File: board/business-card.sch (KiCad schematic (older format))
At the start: 36 parts, among them J1 Conn_01x06, SW1 SW_SPDT, SW2 Mutual_Capacitance_Button, SW3 Mutual_Capacitance_Button, SW4 Mutual_Capacitance_Button, SW5 Mutual_Capacitance_Button, SW6 Mutual_Capacitance_Button, SW7 Mutual_Capacitance_Button, U1 ATtiny1616-S

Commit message: Added through board footprint for XZCBD led.
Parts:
- BT1: mfg1 (none) -> Renata; mfg1pn (none) -> CR2016 MFR SM
- D1, D10, D11, D12, D13, D14, D15, D16, D17, D18, D19, D2, D20, D21, D22, D23, D24, D25, D3, D4, D5, D6, D7, D8, D9: footprint LED_SMD:LED_0603_1608Metric -> business-card:XZCBD53W-6_through_board_mount
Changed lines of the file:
@@
 F 2 "business-card:CR2016_MFR_SM_through_board_mount" V 1200 2360 50  0001 C CNN
 F 3 "~" V 1200 2360 50  0001 C CNN
+F 4 "Renata" H 1200 2300 50  0001 C CNN "mfg1"
+F 5 "CR2016 MFR SM" H 1200 2300 50  0001 C CNN "mfg1pn"
 	1    1200 2300
 	1    0    0    -1
@@
 F 0 "D1" H 8093 1566 50  0000 C CNN
 F 1 "LED" H 8093 1475 50  0000 C CNN
-F 2 "LED_SMD:LED_0603_1608Metric" H 8100 1350 50  0001 C CNN
+F 2 "business-card:XZCBD53W-6_through_board_mount" H 8100 1350 50  0001 C CNN
 F 3 "~" H 8100 1350 50  0001 C CNN
 F 4 "SunLED" H 8100 1350 50  0001 C CNN "mfg1"
@@
 F 0 "D3" H 8493 1566 50  0000 C CNN
 F 1 "LED" H 8493 1475 50  0000 C CNN
-F 2 "LED_SMD:LED_0603_1608Metric" H 8500 1350 50  0001 C CNN
+F 2 "business-card:XZCBD53W-6_through_board_mount" H 8500 1350 50  0001 C CNN
 F 3 "~" H 8500 1350 50  0001 C CNN
 F 4 "SunLED" H 8500 1350 50  0001 C CNN "mfg1"
@@
 F 0 "D5" H 8893 1566 50  0000 C CNN
 F 1 "LED" H 8893 1475 50  0000 C CNN
-F 2 "LED_SMD:LED_0603_1608Metric" H 8900 1350 50  0001 C CNN
+F 2 "business-card:XZCBD53W-6_through_board_mount" H 8900 1350 50  0001 C CNN
 F 3 "~" H 8900 1350 50  0001 C CNN
 F 4 "SunLED" H 8900 1350 50  0001 C CNN "mfg1"
@@
 F 0 "D7" H 9293 1566 50  0000 C CNN
 F 1 "LED" H 9293 1475 50  0000 C CNN
-F 2 "LED_SMD:LED_0603_1608Metric" H 9300 1350 50  0001 C CNN
+F 2 "business-card:XZCBD53W-6_through_board_mount" H 9300 1350 50  0001 C CNN
 F 3 "~" H 9300 1350 50  0001 C CNN
 F 4 "SunLED" H 9300 1350 50  0001 C CNN "mfg1"
@@
 F 0 "D2" H 8093 2716 50  0000 C CNN
 F 1 "LED" H 8093 2625 50  0000 C CNN
-F 2 "LED_SMD:LED_0603_1608Metric" H 8100 2500 50  0001 C CNN
+F 2 "business-card:XZCBD53W-6_through_board_mount" H 8100 2500 50  0001 C CNN
 F 3 "~" H 8100 2500 50  0001 C CNN
 F 4 "SunLED" H 8100 2500 50  0001 C CNN "mfg1"
@@
 F 0 "D4" H 8493 2716 50  0000 C CNN
 F 1 "LED" H 8493 2625 50  0000 C CNN
-F 2 "LED_SMD:LED_0603_1608Metric" H 8500 2500 50  0001 C CNN
+F 2 "business-card:XZCBD53W-6_through_board_mount" H 8500 2500 50  0001 C CNN
 F 3 "~" H 8500 2500 50  0001 C CNN
 F 4 "SunLED" H 8500 2500 50  0001 C CNN "mfg1"
@@
 F 0 "D6" H 8893 2716 50  0000 C CNN
 F 1 "LED" H 8893 2625 50  0000 C CNN
-F 2 "LED_SMD:LED_0603_1608Metric" H 8900 2500 50  0001 C CNN
+F 2 "business-card:XZCBD53W-6_through_board_mount" H 8900 2500 50  0001 C CNN
 F 3 "~" H 8900 2500 50  0001 C CNN
 F 4 "SunLED" H 8900 2500 50  0001 C CNN "mfg1"
@@
 F 0 "D8" H 9293 2716 50  0000 C CNN
 F 1 "LED" H 9293 2625 50  0000 C CNN
-F 2 "LED_SMD:LED_0603_1608Metric" H 9300 2500 50  0001 C CNN
+F 2 "business-card:XZCBD53W-6_through_board_mount" H 9300 2500 50  0001 C CNN
 F 3 "~" H 9300 2500 50  0001 C CNN
 F 4 "SunLED" H 9300 2500 50  0001 C CNN "mfg1"
@@
 F 0 "D9" H 8093 3816 50  0000 C CNN
 F 1 "LED" H 8093 3725 50  0000 C CNN
-F 2 "LED_SMD:LED_0603_1608Metric" H 8100 3600 50  0001 C CNN
+F 2 "business-card:XZCBD53W-6_through_board_mount" H 8100 3600 50  0001 C CNN
 F 3 "~" H 8100 3600 50  0001 C CNN
 F 4 "SunLED" H 8100 3600 50  0001 C CNN "mfg1"
@@
 F 0 "D11" H 8493 3816 50  0000 C CNN
 F 1 "LED" H 8493 3725 50  0000 C CNN
-F 2 "LED_SMD:LED_0603_1608Metric" H 8500 3600 50  0001 C CNN
+F 2 "business-card:XZCBD53W-6_through_board_mount" H 8500 3600 50  0001 C CNN
 F 3 "~" H 8500 3600 50  0001 C CNN
 F 4 "SunLED" H 8500 3600 50  0001 C CNN "mfg1"
@@
 F 0 "D13" H 8893 3816 50  0000 C CNN
 F 1 "LED" H 8893 3725 50  0000 C CNN
-F 2 "LED_SMD:LED_0603_1608Metric" H 8900 3600 50  0001 C CNN
+F 2 "business-card:XZCBD53W-6_through_board_mount" H 8900 3600 50  0001 C CNN
 F 3 "~" H 8900 3600 50  0001 C CNN
 F 4 "SunLED" H 8900 3600 50  0001 C CNN "mfg1"
@@
 F 0 "D15" H 9293 3816 50  0000 C CNN
 F 1 "LED" H 9293 3725 50  0000 C CNN
-F 2 "LED_SMD:LED_0603_1608Metric" H 9300 3600 50  0001 C CNN
+F 2 "business-card:XZCBD53W-6_through_board_mount" H 9300 3600 50  0001 C CNN
 F 3 "~" H 9300 3600 50  0001 C CNN
 F 4 "SunLED" H 9300 3600 50  0001 C CNN "mfg1"
@@
 F 0 "D10" H 8093 4916 50  0000 C CNN
 F 1 "LED" H 8093 4825 50  0000 C CNN
-F 2 "LED_SMD:LED_0603_1608Metric" H 8100 4700 50  0001 C CNN
+F 2 "business-card:XZCBD53W-6_through_board_mount" H 8100 4700 50  0001 C CNN
 F 3 "~" H 8100 4700 50  0001 C CNN
 F 4 "SunLED" H 8100 4700 50  0001 C CNN "mfg1"
@@
 F 0 "D12" H 8493 4916 50  0000 C CNN
 F 1 "LED" H 8493 4825 50  0000 C CNN
-F 2 "LED_SMD:LED_0603_1608Metric" H 8500 4700 50  0001 C CNN
+F 2 "business-card:XZCBD53W-6_through_board_mount" H 8500 4700 50  0001 C CNN
 F 3 "~" H 8500 4700 50  0001 C CNN
 F 4 "SunLED" H 8500 4700 50  0001 C CNN "mfg1"
@@
 F 0 "D14" H 8893 4916 50  0000 C CNN
 F 1 "LED" H 8893 4825 50  0000 C CNN
-F 2 "LED_SMD:LED_0603_1608Metric" H 8900 4700 50  0001 C CNN
+F 2 "business-card:XZCBD53W-6_through_board_mount" H 8900 4700 50  0001 C CNN
 F 3 "~" H 8900 4700 50  0001 C CNN
 F 4 "SunLED" H 8900 4700 50  0001 C CNN "mfg1"
@@
 F 0 "D16" H 9293 4916 50  0000 C CNN
 F 1 "LED" H 9293 4825 50  0000 C CNN
-F 2 "LED_SMD:LED_0603_1608Metric" H 9300 4700 50  0001 C CNN
+F 2 "business-card:XZCBD53W-6_through_board_mount" H 9300 4700 50  0001 C CNN
 F 3 "~" H 9300 4700 50  0001 C CNN
 F 4 "SunLED" H 9300 4700 50  0001 C CNN "mfg1"
@@
 F 0 "D21" H 9693 1566 50  0000 C CNN
 F 1 "LED" H 9693 1475 50  0000 C CNN
-F 2 "LED_SMD:LED_0603_1608Metric" H 9700 1350 50  0001 C CNN
+F 2 "business-card:XZCBD53W-6_through_board_mount" H 9700 1350 50  0001 C CNN
 F 3 "~" H 9700 1350 50  0001 C CNN
 F 4 "SunLED" H 9700 1350 50  0001 C CNN "mfg1"
@@
 F 0 "D22" H 9693 2716 50  0000 C CNN
 F 1 "LED" H 9693 2625 50  0000 C CNN
-F 2 "LED_SMD:LED_0603_1608Metric" H 9700 2500 50  0001 C CNN
+F 2 "business-card:XZCBD53W-6_through_board_mount" H 9700 2500 50  0001 C CNN
 F 3 "~" H 9700 2500 50  0001 C CNN
 F 4 "SunLED" H 9700 2500 50  0001 C CNN "mfg1"
@@
 F 0 "D23" H 9693 3816 50  0000 C CNN
 F 1 "LED" H 9693 3725 50  0000 C CNN
-F 2 "LED_SMD:LED_0603_1608Metric" H 9700 3600 50  0001 C CNN
+F 2 "business-card:XZCBD53W-6_through_board_mount" H 9700 3600 50  0001 C CNN
 F 3 "~" H 9700 3600 50  0001 C CNN
 F 4 "SunLED" H 9700 3600 50  0001 C CNN "mfg1"
@@
 F 0 "D24" H 9693 4916 50  0000 C CNN
 F 1 "LED" H 9693 4825 50  0000 C CNN
-F 2 "LED_SMD:LED_0603_1608Metric" H 9700 4700 50  0001 C CNN
+F 2 "business-card:XZCBD53W-6_through_board_mount" H 9700 4700 50  0001 C CNN
 F 3 "~" H 9700 4700 50  0001 C CNN
 F 4 "SunLED" H 9700 4700 50  0001 C CNN "mfg1"
@@
 F 0 "D17" H 8093 6016 50  0000 C CNN
 F 1 "LED" H 8093 5925 50  0000 C CNN
-F 2 "LED_SMD:LED_0603_1608Metric" H 8100 5800 50  0001 C CNN
+F 2 "business-card:XZCBD53W-6_through_board_mount" H 8100 5800 50  0001 C CNN
 F 3 "~" H 8100 5800 50  0001 C CNN
 F 4 "SunLED" H 8100 5800 50  0001 C CNN "mfg1"
@@
 F 0 "D18" H 8493 6016 50  0000 C CNN
 F 1 "LED" H 8493 5925 50  0000 C CNN
-F 2 "LED_SMD:LED_0603_1608Metric" H 8500 5800 50  0001 C CNN
+F 2 "business-card:XZCBD53W-6_through_board_mount" H 8500 5800 50  0001 C CNN
 F 3 "~" H 8500 5800 50  0001 C CNN
 F 4 "SunLED" H 8500 5800 50  0001 C CNN "mfg1"
@@
 F 0 "D19" H 8893 6016 50  0000 C CNN
 F 1 "LED" H 8893 5925 50  0000 C CNN
-F 2 "LED_SMD:LED_0603_1608Metric" H 8900 5800 50  0001 C CNN
+F 2 "business-card:XZCBD53W-6_through_board_mount" H 8900 5800 50  0001 C CNN
 F 3 "~" H 8900 5800 50  0001 C CNN
 F 4 "SunLED" H 8900 5800 50  0001 C CNN "mfg1"
@@
 F 0 "D20" H 9293 6016 50  0000 C CNN
 F 1 "LED" H 9293 5925 50  0000 C CNN
-F 2 "LED_SMD:LED_0603_1608Metric" H 9300 5800 50  0001 C CNN
+F 2 "business-card:XZCBD53W-6_through_board_mount" H 9300 5800 50  0001 C CNN
 F 3 "~" H 9300 5800 50  0001 C CNN
 F 4 "SunLED" H 9300 5800 50  0001 C CNN "mfg1"
@@
 F 0 "D25" H 9693 6016 50  0000 C CNN
 F 1 "LED" H 9693 5925 50  0000 C CNN
-F 2 "LED_SMD:LED_0603_1608Metric" H 9700 5800 50  0001 C CNN
+F 2 "business-card:XZCBD53W-6_through_board_mount" H 9700 5800 50  0001 C CNN
 F 3 "~" H 9700 5800 50  0001 C CNN
 F 4 "SunLED" H 9700 5800 50  0001 C CNN "mfg1"

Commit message: Added 0603 through board mount, arranged leds in grid.
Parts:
- C2: footprint Capacitor_SMD:C_0603_1608Metric -> business-card:0603_through_board_mount
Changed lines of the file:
@@
 F 0 "C2" V 4702 3400 50  0000 C CNN
 F 1 "0.1 uF" V 4611 3400 50  0000 C CNN
-F 2 "Capacitor_SMD:C_0603_1608Metric" H 4488 3250 50  0001 C CNN
+F 2 "business-card:0603_through_board_mount" H 4488 3250 50  0001 C CNN
 F 3 "~" H 4450 3400 50  0001 C CNN
 	1    4450 3400

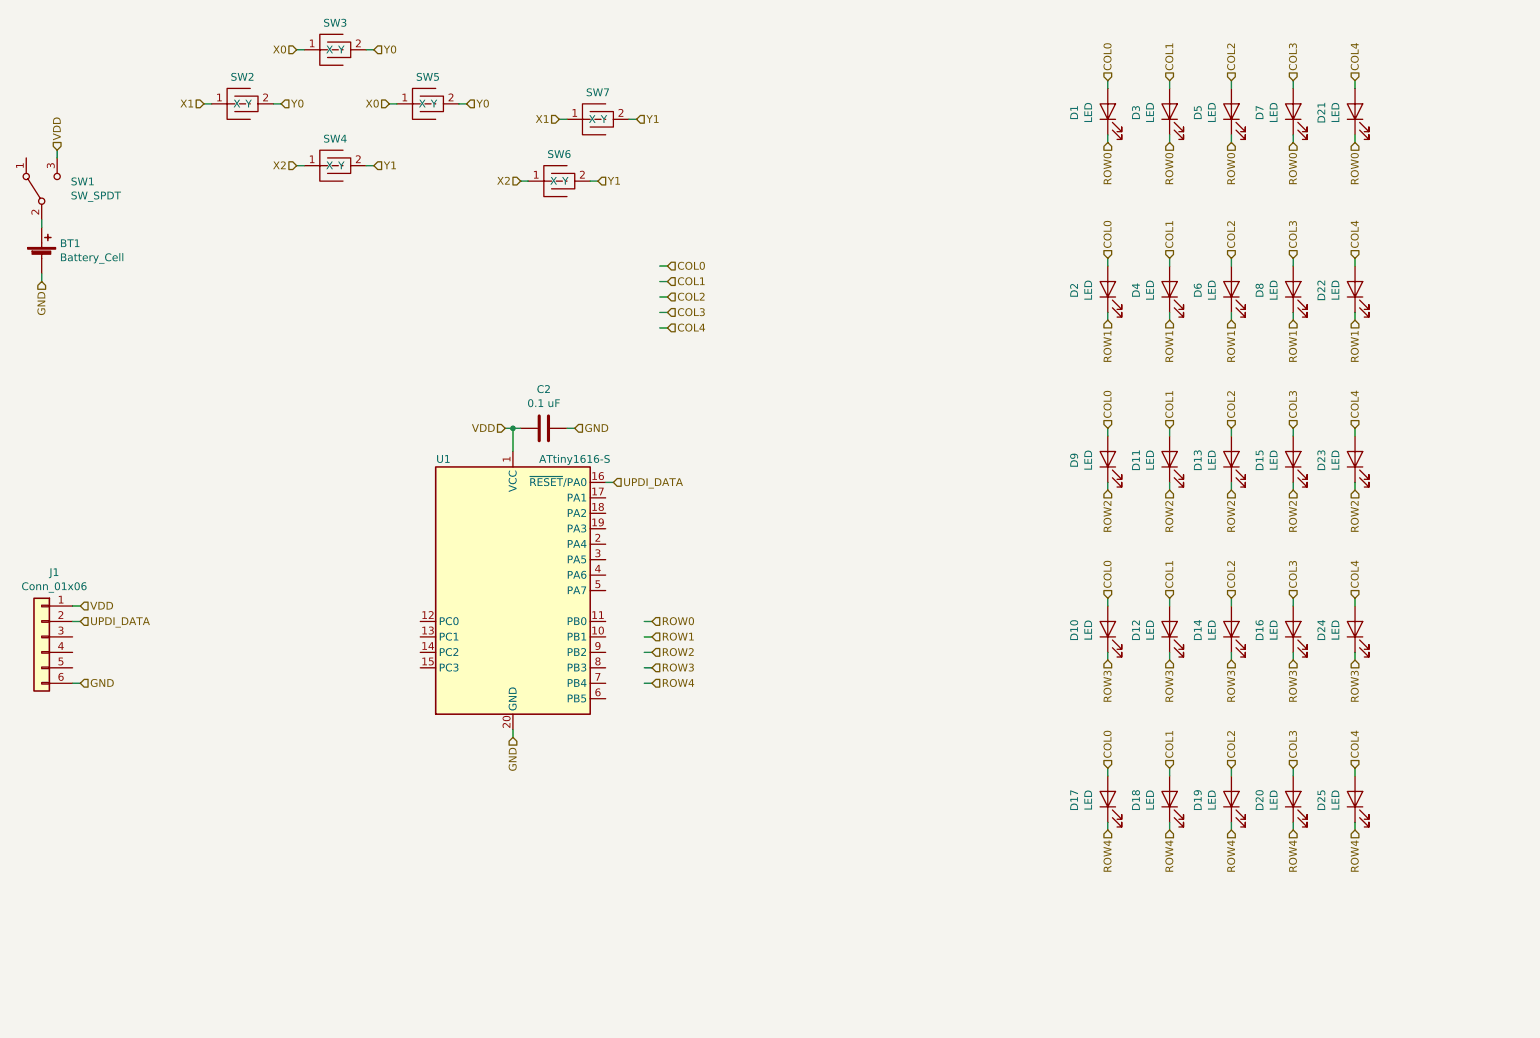
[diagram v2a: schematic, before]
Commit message: Added another row and column of leds.
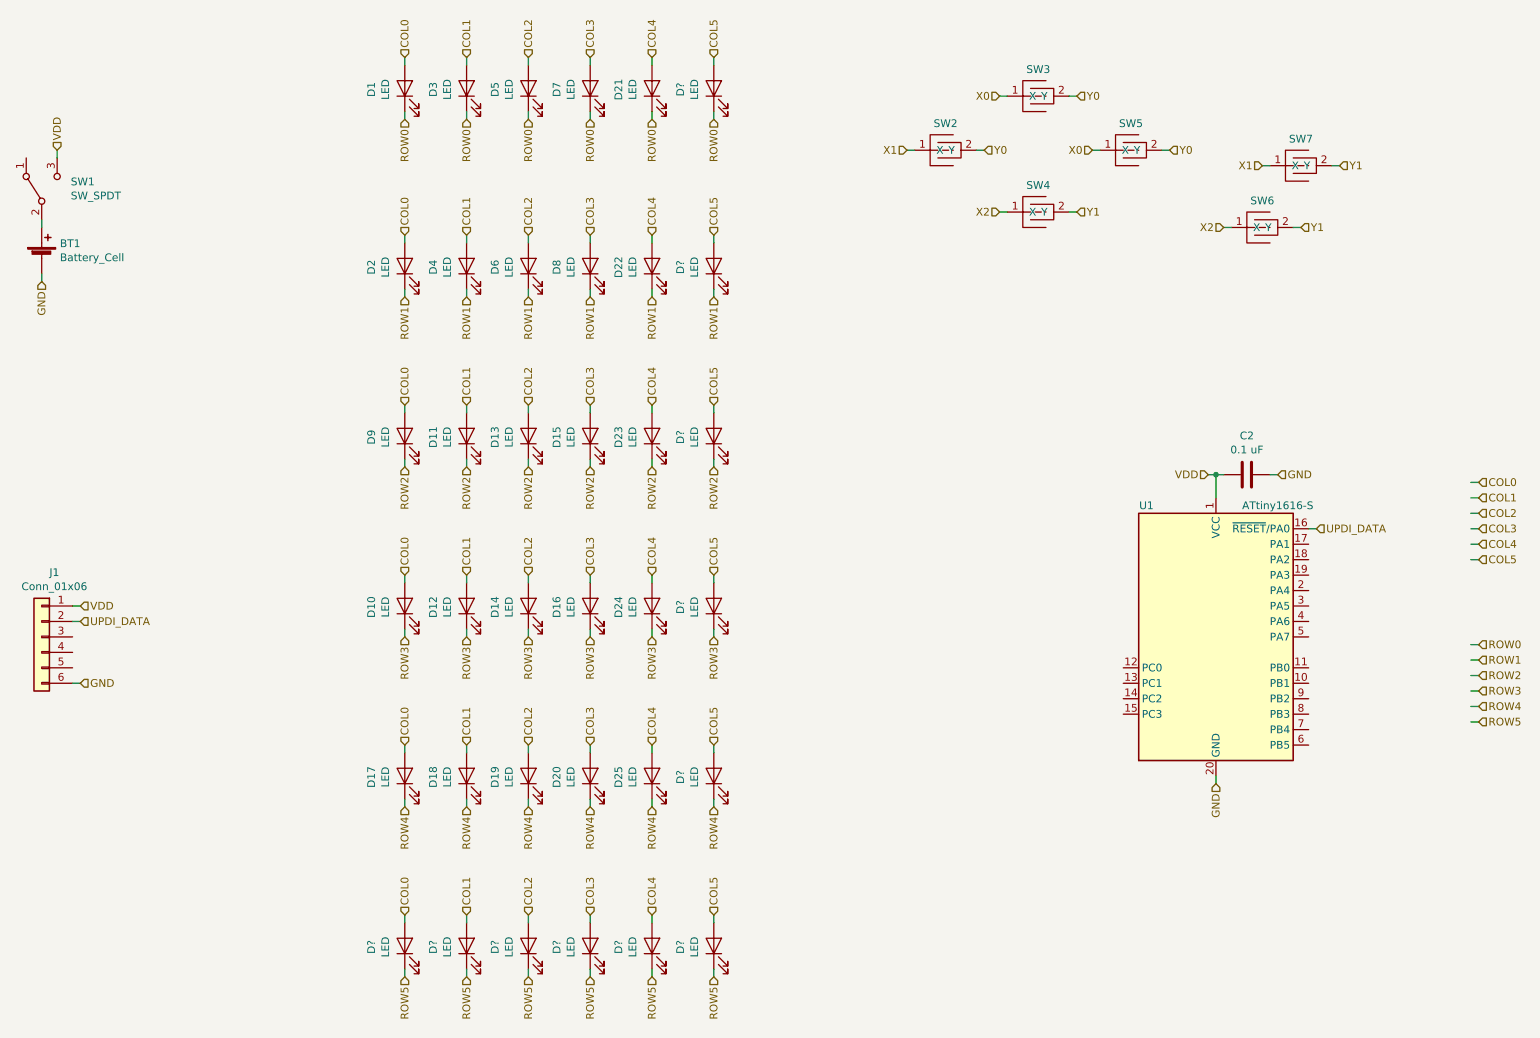
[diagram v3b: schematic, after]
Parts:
- added D? (x11): LED, business-card:XZCBD53W-6_through_board_mount, symbol Device:LED
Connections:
- net labels added: COL5, ROW5
- wire segments 84 -> 108
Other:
- moved on the sheet: C2, D1, D10, D11, D12, D13, D14, D15, D16, D17, D18, D19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
